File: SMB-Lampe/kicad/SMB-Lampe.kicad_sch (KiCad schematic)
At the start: 1 part, among them SW1 SW_SPST

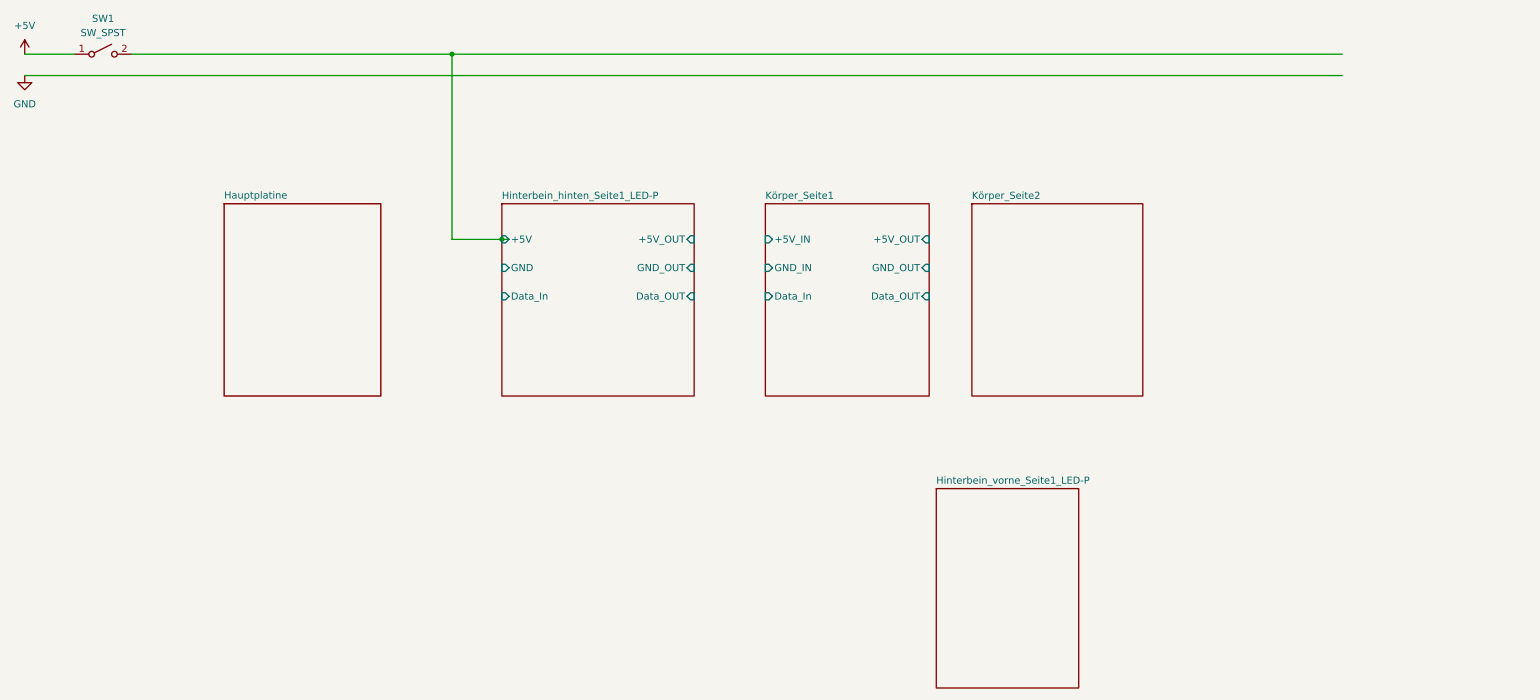
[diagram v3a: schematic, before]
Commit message: Alle Platinen erstellt
Alle Platinen wurden im Projekt einzeln erstellt.
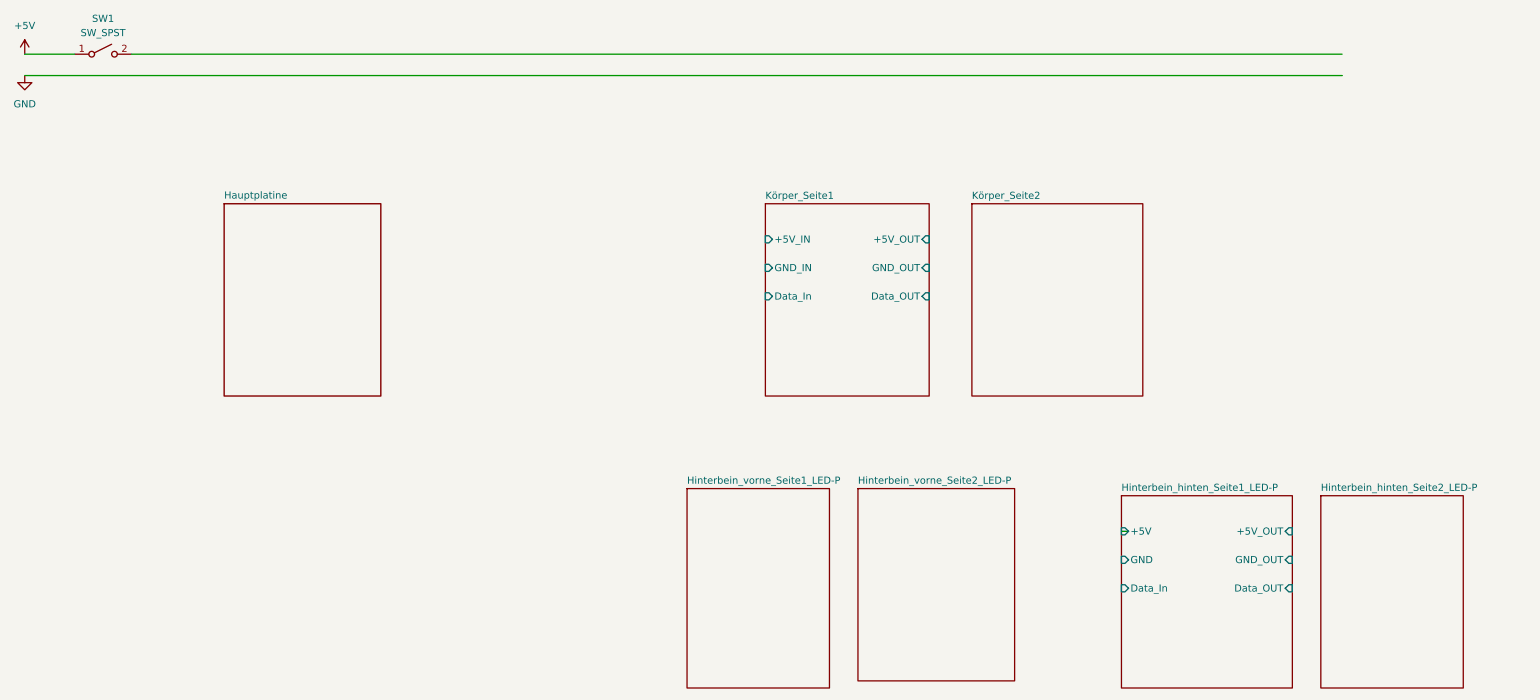
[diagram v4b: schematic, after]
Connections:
- net Hinterbein_hinten_Seite1_LED-P/+5V: no longer SW1.2 (B)
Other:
- added sheet Hinterbein_hinten_Seite2_LED-P (Hinterbein_hinten_Seite2_LED-P/Hinterbein_hinten_Seite2_LED-P.kicad_sch)
- added sheet Hinterbein_vorne_Seite2_LED-P (Hinterbein_vorne_Seite2_LED-P/Hinterbein_vorne_Seite2_LED-P.kicad_sch)
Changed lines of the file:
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@@
 	(generator_version "9.0")
 	(paper "A4")
-	(junction
-		(at 101.6 25.4)
-		(diameter 0)
-		(color 0 0 0 0)
-	)
-	(junction
-		(at 110.49 58.42)
-		(diameter 0)
-		(color 0 0 0 0)
-	)
 	(wire
 		(pts
-			(xy 101.6 25.4) (xy 260.35 25.4)
+			(xy 44.45 25.4) (xy 260.35 25.4)
 		)
 		(stroke
@@
 	(wire
 		(pts
-			(xy 101.6 25.4) (xy 101.6 58.42)
+			(xy 25.4 29.21) (xy 260.35 29.21)
 		)
 		(stroke
@@
 	(wire
 		(pts
-			(xy 25.4 29.21) (xy 260.35 29.21)
-		)
-		(stroke
-			(width 0)
-			(type default)
-		)
-	)
-	(wire
-		(pts
-			(xy 110.49 58.42) (xy 111.76 58.42)
-		)
-		(stroke
-			(width 0)
-			(type default)
-		)
-	)
-	(wire
-		(pts
-			(xy 44.45 25.4) (xy 101.6 25.4)
-		)
-		(stroke
-			(width 0)
-			(type default)
-		)
-	)
-	(wire
-		(pts
-			(xy 101.6 58.42) (xy 110.49 58.42)
+			(xy 220.98 110.49) (xy 222.25 110.49)
 		)
 		(stroke
@@
 	)
 	(sheet
-		(at 110.49 52.07)
-		(size 34.29 34.29)
+		(at 173.99 102.87)
+		(size 27.94 34.29)
 		(exclude_from_sim no)
 		(in_bom yes)
@@
 			(color 0 0 0 0.0000)
 		)
+		(property "Sheetname" "Hinterbein_vorne_Seite2_LED-P"
+			(at 173.99 102.1584 0)
+			(effects
+				(font
+					(size 1.27 1.27)
+				)
+				(justify left bottom)
+			)
+		)
+		(property "Sheetfile" "Hinterbein_vorne_Seite2_LED-P/Hinterbein_vorne_Seite2_LED-P.kicad_sch"
+			(at 173.99 137.7446 0)
+			(effects
+				(font
+					(size 1.27 1.27)
+				)
+				(justify left top)
+				(hide yes)
+			)
+		)
+		(instances
+			(project "SMB-Lampe"
+				(path "/4831ca1b-de6c-4f01-b2f4-c7955e9e85c5"
+					(page "8")
+				)
+			)
+		)
+	)
+	(sheet
+		(at 220.98 104.14)
+		(size 30.48 34.29)
+		(exclude_from_sim no)
+		(in_bom yes)
+		(on_board yes)
+		(dnp no)
+		(fields_autoplaced yes)
+		(stroke
+			(width 0.1524)
+			(type solid)
+		)
+		(fill
+			(color 0 0 0 0.0000)
+		)
 		(property "Sheetname" "Hinterbein_hinten_Seite1_LED-P"
-			(at 110.49 51.3584 0)
+			(at 220.98 103.4284 0)
 			(effects
 				(font
@@
 		)
 		(property "Sheetfile" "Hinterbein_hinten_Seite1_LED-P/Hinterbein_hinten_Seite1_LED-P.kicad_sch"
-			(at 110.49 86.9446 0)
+			(at 220.98 139.0146 0)
 			(effects
 				(font
@@
 		)
 		(pin "+5V" input
-			(at 110.49 58.42 180)
+			(at 220.98 110.49 180)
 			(effects
 				(font
@@
 		)
 		(pin "GND" input
-			(at 110.49 63.5 180)
+			(at 220.98 115.57 180)
 			(effects
 				(font
@@
 		)
 		(pin "+5V_OUT" input
-			(at 144.78 58.42 0)
+			(at 251.46 110.49 0)
 			(effects
 				(font
@@
 		)
 		(pin "Data_In" input
-			(at 110.49 68.58 180)
+			(at 220.98 120.65 180)
 			(effects
 				(font
@@
 		)
 		(pin "Data_OUT" input
-			(at 144.78 68.58 0)
+			(at 251.46 120.65 0)
 			(effects
 				(font
@@
 		)
 		(pin "GND_OUT" input
-			(at 144.78 63.5 0)
+			(at 251.46 115.57 0)
 			(effects
 				(font
@@
 	)
 	(sheet
-		(at 187.96 102.87)
+		(at 143.51 102.87)
 		(size 25.4 35.56)
 		(exclude_from_sim no)
@@
 		)
 		(property "Sheetname" "Hinterbein_vorne_Seite1_LED-P"
-			(at 187.96 102.1584 0)
+			(at 143.51 102.1584 0)
 			(effects
 				(font
@@
 		)
 		(property "Sheetfile" "Hinterbein_vorne_Seite1_LED-P/Hinterbein_vorne_Seite1_LED-P.kicad_sch"
-			(at 187.96 139.0146 0)
+			(at 143.51 139.0146 0)
 			(effects
 				(font
@@
 			(project "SMB-Lampe"
 				(path "/4831ca1b-de6c-4f01-b2f4-c7955e9e85c5"
-					(page "4")
+					(page "7")
 				)
 			)
@@
 				)
 			)
+		)
+	)
+	(sheet
+		(at 256.54 104.14)
+		(size 25.4 34.29)
+		(exclude_from_sim no)
+		(in_bom yes)
+		(on_board yes)
+		(dnp no)
+		(fields_autoplaced yes)
+		(stroke
+			(width 0.1524)
+			(type solid)
+		)
+		(fill
+			(color 0 0 0 0.0000)
+		)
+		(property "Sheetname" "Hinterbein_hinten_Seite2_LED-P"
+			(at 256.54 103.4284 0)
+			(effects
+				(font
+					(size 1.27 1.27)
+				)
+				(justify left bottom)
+			)
+		)
+		(property "Sheetfile" "Hinterbein_hinten_Seite2_LED-P/Hinterbein_hinten_Seite2_LED-P.kicad_sch"
+			(at 256.54 139.0146 0)
+			(effects
+				(font
+					(size 1.27 1.27)
+				)
+				(justify left top)
+				(hide yes)
+			)
+		)
+		(instances
+			(project "SMB-Lampe"
+				(path "/4831ca1b-de6c-4f01-b2f4-c7955e9e85c5"
+					(page "4")
+				)
+			)

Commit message: Alle LEDs nochmal richtig angeschlossen
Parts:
- added P1: USB_C_Plug_USB2.0, symbol Connector:USB_C_Plug_USB2.0
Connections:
- net GND: now also P1.A1 (GND), P1.A12 (GND), P1.B1 (GND), P1.B12 (GND)
- net Körper_Seite1/+5V_IN: now also SW1.2 (B)
- net +5V: no longer names the net of SW1.1 (A)
- net +5V: now also P1.A4 (VBUS), P1.A5 (CC), P1.A9 (VBUS), P1.B4 (VBUS), P1.B9 (VBUS)
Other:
- sheet Körper_Seite1: file Körper_Seite1/KörperKörper_Seite1.kicad_sch -> Körper_Seite1/Körper_Seite1.kicad_sch
- moved on the sheet: SW1
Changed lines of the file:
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@@
 	(generator_version "9.0")
 	(paper "A4")
-	(wire
-		(pts
-			(xy 44.45 25.4) (xy 260.35 25.4)
-		)
-		(stroke
-			(width 0)
-			(type default)
-		)
-	)
-	(wire
-		(pts
-			(xy 25.4 25.4) (xy 34.29 25.4)
-		)
-		(stroke
-			(width 0)
-			(type default)
-		)
-	)
-	(wire
-		(pts
-			(xy 25.4 29.21) (xy 260.35 29.21)
-		)
-		(stroke
-			(width 0)
-			(type default)
-		)
-	)
-	(wire
-		(pts
-			(xy 220.98 110.49) (xy 222.25 110.49)
-		)
-		(stroke
-			(width 0)
-			(type default)
+	(junction
+		(at 35.56 66.04)
+		(diameter 0)
+		(color 0 0 0 0)
+	)
+	(junction
+		(at 50.8 27.94)
+		(diameter 0)
+		(color 0 0 0 0)
+	)
+	(junction
+		(at 139.7 25.4)
+		(diameter 0)
+		(color 0 0 0 0)
+	)
+	(wire
+		(pts
+			(xy 139.7 25.4) (xy 139.7 58.42)
+		)
+		(stroke
+			(width 0)
+			(type default)
+		)
+	)
+	(wire
+		(pts
+			(xy 53.34 29.21) (xy 260.35 29.21)
+		)
+		(stroke
+			(width 0)
+			(type default)
+		)
+	)
+	(wire
+		(pts
+			(xy 88.9 25.4) (xy 139.7 25.4)
+		)
+		(stroke
+			(width 0)
+			(type default)
+		)
+	)
+	(wire
+		(pts
+			(xy 35.56 66.04) (xy 53.34 66.04)
+		)
+		(stroke
+			(width 0)
+			(type default)
+		)
+	)
+	(wire
+		(pts
+			(xy 50.8 25.4) (xy 78.74 25.4)
+		)
+		(stroke
+			(width 0)
+			(type default)
+		)
+	)
+	(wire
+		(pts
+			(xy 139.7 58.42) (xy 157.48 58.42)
+		)
+		(stroke
+			(width 0)
+			(type default)
+		)
+	)
+	(wire
+		(pts
+			(xy 50.8 27.94) (xy 50.8 33.02)
+		)
+		(stroke
+			(width 0)
+			(type default)
+		)
+	)
+	(wire
+		(pts
+			(xy 139.7 25.4) (xy 260.35 25.4)
+		)
+		(stroke
+			(width 0)
+			(type default)
+		)
+	)
+	(wire
+		(pts
+			(xy 50.8 25.4) (xy 50.8 27.94)
+		)
+		(stroke
+			(width 0)
+			(type default)
+		)
+	)
+	(wire
+		(pts
+			(xy 53.34 29.21) (xy 53.34 66.04)
+		)
+		(stroke
+			(width 0)
+			(type default)
+		)
+	)
+	(symbol
+		(lib_id "Connector:USB_C_Plug_USB2.0")
+		(at 35.56 43.18 0)
+		(unit 1)
+		(exclude_from_sim no)
+		(in_bom yes)
+		(on_board yes)
+		(dnp no)
+		(fields_autoplaced yes)
+		(property "Reference" "P1"
+			(at 35.56 20.32 0)
+			(effects
+				(font
+					(size 1.27 1.27)
+				)
+			)
+		)
+		(property "Value" "USB_C_Plug_USB2.0"
+			(at 35.56 22.86 0)
+			(effects
+				(font
+					(size 1.27 1.27)
+				)
+			)
+		)
+		(property "Footprint" ""
+			(at 39.37 43.18 0)
+			(effects
+				(font
+					(size 1.27 1.27)
+				)
+				(hide yes)
+			)
+		)
+		(property "Datasheet" "https://www.usb.org/sites/default/files/documents/usb_type-c.zip"
+			(at 39.37 43.18 0)
+			(effects
+				(font
+					(size 1.27 1.27)
+				)
+				(hide yes)
+			)
+		)
+		(property "Description" "USB 2.0-only Type-C Plug connector"
+			(at 35.56 43.18 0)
+			(effects
+				(font
+					(size 1.27 1.27)
+				)
+				(hide yes)
+			)
+		)
+		(pin "A4"
+		)
+		(pin "A6"
+		)
+		(pin "B9"
+		)
+		(pin "S1"
+		)
+		(pin "A5"
+		)
+		(pin "A1"
+		)
+		(pin "B1"
+		)
+		(pin "B12"
+		)
+		(pin "B4"
+		)
+		(pin "A7"
+		)
+		(pin "A9"
+		)
+		(pin "A12"
+		)
+		(pin "B5"
+		)
+		(instances
+			(project ""
+				(path "/4831ca1b-de6c-4f01-b2f4-c7955e9e85c5"
+					(reference "P1")
+					(unit 1)
+				)
+			)
+		)
+	)
+	(symbol
+		(lib_id "power:GND")
+		(at 35.56 66.04 0)
+		(unit 1)
+		(exclude_from_sim no)
+		(in_bom yes)
+		(on_board yes)
+		(dnp no)
+		(fields_autoplaced yes)
+		(property "Reference" "#PWR01"
+			(at 35.56 72.39 0)
+			(effects
+				(font
+					(size 1.27 1.27)
+				)
+				(hide yes)
+			)
+		)
+		(property "Value" "GND"
+			(at 35.56 71.12 0)
+			(effects
+				(font
+					(size 1.27 1.27)
+				)
+			)
+		)
+		(property "Footprint" ""
+			(at 35.56 66.04 0)
+			(effects
+				(font
+					(size 1.27 1.27)
+				)
+				(hide yes)
+			)
+		)
+		(property "Datasheet" ""
+			(at 35.56 66.04 0)
+			(effects
+				(font
+					(size 1.27 1.27)
+				)
+				(hide yes)
+			)
+		)
+		(property "Description" "Power symbol creates a global label with name \"GND\" , ground"
+			(at 35.56 66.04 0)
+			(effects
+				(font
+					(size 1.27 1.27)
+				)
+				(hide yes)
+			)
+		)
+		(pin "1"
+		)
+		(instances
+			(project ""
+				(path "/4831ca1b-de6c-4f01-b2f4-c7955e9e85c5"
+					(reference "#PWR01")
+					(unit 1)
+				)
+			)
 		)
 	)
 	(symbol
 		(lib_id "Switch:SW_SPST")
-		(at 39.37 25.4 0)
+		(at 83.82 25.4 0)
 		(unit 1)
 		(exclude_from_sim no)
@@
 		(fields_autoplaced yes)
 		(property "Reference" "SW1"
-			(at 39.37 19.05 0)
+			(at 83.82 19.05 0)
 			(effects
 				(font
@@
 		)
 		(property "Value" "SW_SPST"
-			(at 39.37 21.59 0)
+			(at 83.82 21.59 0)
 			(effects
 				(font
@@
 		)
 		(property "Footprint" ""
-			(at 39.37 25.4 0)
+			(at 83.82 25.4 0)
 			(effects
 				(font
@@
 		)
 		(property "Datasheet" "~"
-			(at 39.37 25.4 0)
+			(at 83.82 25.4 0)
 			(effects
 				(font
@@
 		)
 		(property "Description" "Single Pole Single Throw (SPST) switch"
-			(at 39.37 25.4 0)
+			(at 83.82 25.4 0)
 			(effects
 				(font
@@
 				(path "/4831ca1b-de6c-4f01-b2f4-c7955e9e85c5"
 					(reference "SW1")
-					(unit 1)
-				)
-			)
-		)
-	)
-	(symbol
-		(lib_id "power:+5V")
-		(at 25.4 25.4 0)
-		(unit 1)
-		(exclude_from_sim no)
-		(in_bom yes)
-		(on_board yes)
-		(dnp no)
-		(fields_autoplaced yes)
-		(property "Reference" "#PWR01"
-			(at 25.4 29.21 0)
-			(effects
-				(font
-					(size 1.27 1.27)
-				)
-				(hide yes)
-			)
-		)
-		(property "Value" "+5V"
-			(at 25.4 20.32 0)
-			(effects
-				(font
-					(size 1.27 1.27)
-				)
-			)
-		)
-		(property "Footprint" ""
-			(at 25.4 25.4 0)
-			(effects
-				(font
-					(size 1.27 1.27)
-				)
-				(hide yes)
-			)
-		)
-		(property "Datasheet" ""
-			(at 25.4 25.4 0)
-			(effects
-				(font
-					(size 1.27 1.27)
-				)
-				(hide yes)
-			)
-		)
-		(property "Description" "Power symbol creates a global label with name \"+5V\""
-			(at 25.4 25.4 0)
-			(effects
-				(font
-					(size 1.27 1.27)
-				)
-				(hide yes)
-			)
-		)
-		(pin "1"
-		)
-		(instances
-			(project ""
-				(path "/4831ca1b-de6c-4f01-b2f4-c7955e9e85c5"
-					(reference "#PWR01")
-					(unit 1)
-				)
-			)
-		)
-	)
-	(symbol
-		(lib_id "power:GND")
-		(at 25.4 29.21 0)
-		(unit 1)
-		(exclude_from_sim no)
-		(in_bom yes)
-		(on_board yes)
-		(dnp no)
-		(fields_autoplaced yes)
-		(property "Reference" "#PWR02"
-			(at 25.4 35.56 0)
-			(effects
-				(font
-					(size 1.27 1.27)
-				)
-				(hide yes)
-			)
-		)
-		(property "Value" "GND"
-			(at 25.4 34.29 0)
-			(effects
-				(font
-					(size 1.27 1.27)
-				)
-			)
-		)
-		(property "Footprint" ""
-			(at 25.4 29.21 0)
-			(effects
-				(font
-					(size 1.27 1.27)
-				)
-				(hide yes)
-			)
-		)
-		(property "Datasheet" ""
-			(at 25.4 29.21 0)
-			(effects
-				(font
-					(size 1.27 1.27)
-				)
-				(hide yes)
-			)
-		)
-		(property "Description" "Power symbol creates a global label with name \"GND\" , ground"
-			(at 25.4 29.21 0)
-			(effects
-				(font
-					(size 1.27 1.27)
-				)
-				(hide yes)
-			)
-		)
-		(pin "1"
-		)
-		(instances
-			(project ""
-				(path "/4831ca1b-de6c-4f01-b2f4-c7955e9e85c5"
-					(reference "#PWR02")
 					(unit 1)
 				)
@@
 			)
 		)
-		(property "Sheetfile" "Körper_Seite1/KörperKörper_Seite1.kicad_sch"
+		(property "Sheetfile" "Körper_Seite1/Körper_Seite1.kicad_sch"
 			(at 157.48 86.9446 0)
 			(effects

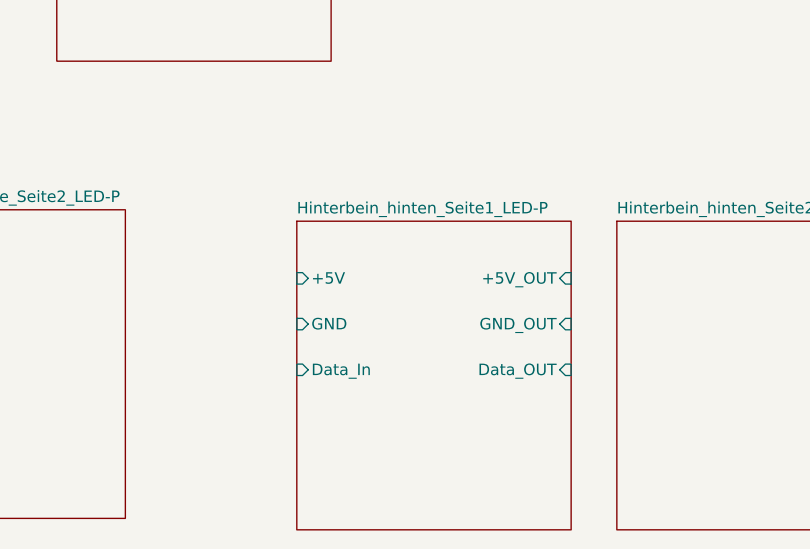
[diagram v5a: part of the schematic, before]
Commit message: Hinterbein Seite 1/2 erstellt
Anschlüsse zwischen den Platinen mit MountingHoles. Eigenes MountingHole Erstellt
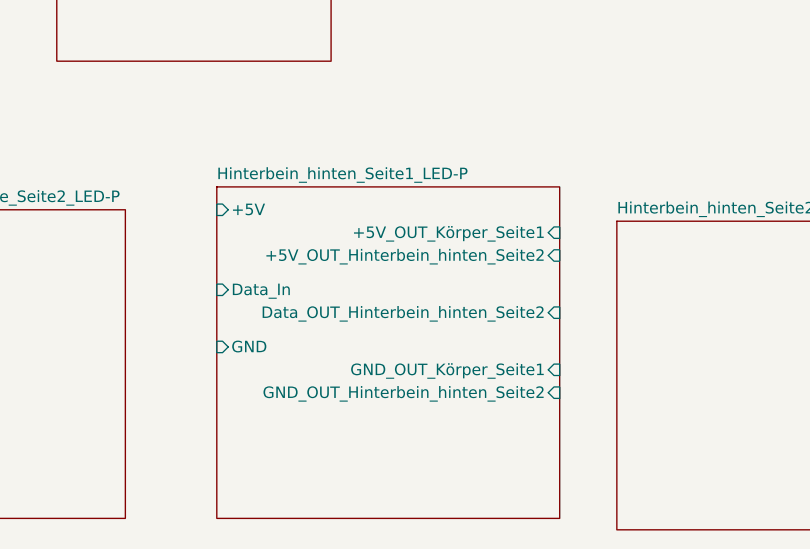
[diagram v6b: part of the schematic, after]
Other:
- sheet Hinterbein_hinten_Seite1_LED-P ports: added +5V_OUT_Hinterbein_hinten_Seite2, +5V_OUT_Körper_Seite1, Data_OUT_Hinterbein_hinten_Seite2, GND_OUT_Hinterbein_hinten_Seite2, GND_OUT_Körper_Seite1; removed +5V_OUT, Data_OUT, GND_OUT
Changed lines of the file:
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@@
 	)
 	(sheet
-		(at 220.98 104.14)
-		(size 30.48 34.29)
+		(at 212.09 100.33)
+		(size 38.1 36.83)
 		(exclude_from_sim no)
 		(in_bom yes)
@@
 		)
 		(property "Sheetname" "Hinterbein_hinten_Seite1_LED-P"
-			(at 220.98 103.4284 0)
+			(at 212.09 99.6184 0)
 			(effects
 				(font
@@
 		)
 		(property "Sheetfile" "Hinterbein_hinten_Seite1_LED-P/Hinterbein_hinten_Seite1_LED-P.kicad_sch"
-			(at 220.98 139.0146 0)
+			(at 212.09 137.7446 0)
 			(effects
 				(font
@@
 		)
 		(pin "+5V" input
-			(at 220.98 110.49 180)
+			(at 212.09 102.87 180)
 			(effects
 				(font
@@
 		)
 		(pin "GND" input
-			(at 220.98 115.57 180)
+			(at 212.09 118.11 180)
 			(effects
 				(font
@@
 			)
 		)
-		(pin "+5V_OUT" input
-			(at 251.46 110.49 0)
+		(pin "+5V_OUT_Hinterbein_hinten_Seite2" input
+			(at 250.19 107.95 0)
 			(effects
 				(font
@@
 		)
 		(pin "Data_In" input
-			(at 220.98 120.65 180)
+			(at 212.09 111.76 180)
 			(effects
 				(font
@@
 			)
 		)
-		(pin "Data_OUT" input
-			(at 251.46 120.65 0)
+		(pin "Data_OUT_Hinterbein_hinten_Seite2" input
+			(at 250.19 114.3 0)
 			(effects
 				(font
@@
 			)
 		)
-		(pin "GND_OUT" input
-			(at 251.46 115.57 0)
+		(pin "GND_OUT_Körper_Seite1" input
+			(at 250.19 120.65 0)
 			(effects
 				(font
+					(size 1.27 1.27)
+				)
+				(justify right)
+			)
+		)
+		(pin "+5V_OUT_Körper_Seite1" input
+			(at 250.19 105.41 0)
+			(effects
+				(font
+					(size 1.27 1.27)
+				)
+				(justify right)
+			)
+		)
+		(pin "GND_OUT_Hinterbein_hinten_Seite2" input
+			(at 250.19 123.19 0)
+			(effects
+				(font
